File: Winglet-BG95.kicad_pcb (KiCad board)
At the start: 4 copper layers, 30 x 47.6 mm, 43 parts, among them J1 2337019-1, J2 2337019-1, J3 NSIM-16-B, M1 PTH_M2.5, M2 PTH_M2.5, Q1 DMG1012UW-7, Q2 DMG1012UW-7, U1 BG95M1LA, U2 MFF2-SIM, U3 24AA01T-I/OT, U4 FXLA108BQX

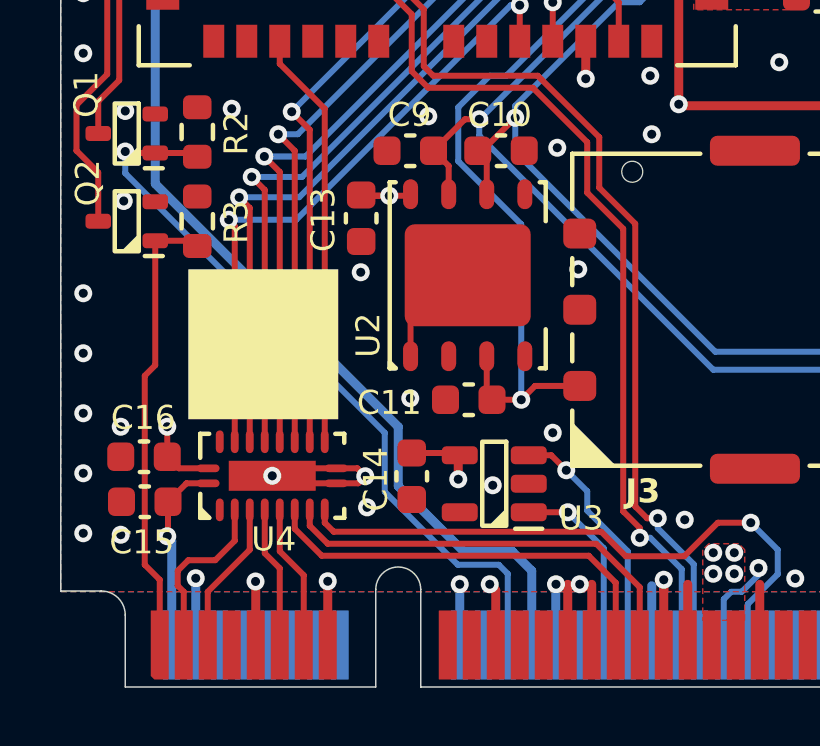
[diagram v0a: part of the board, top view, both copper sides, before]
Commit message: Update export scripts
Change DNF options
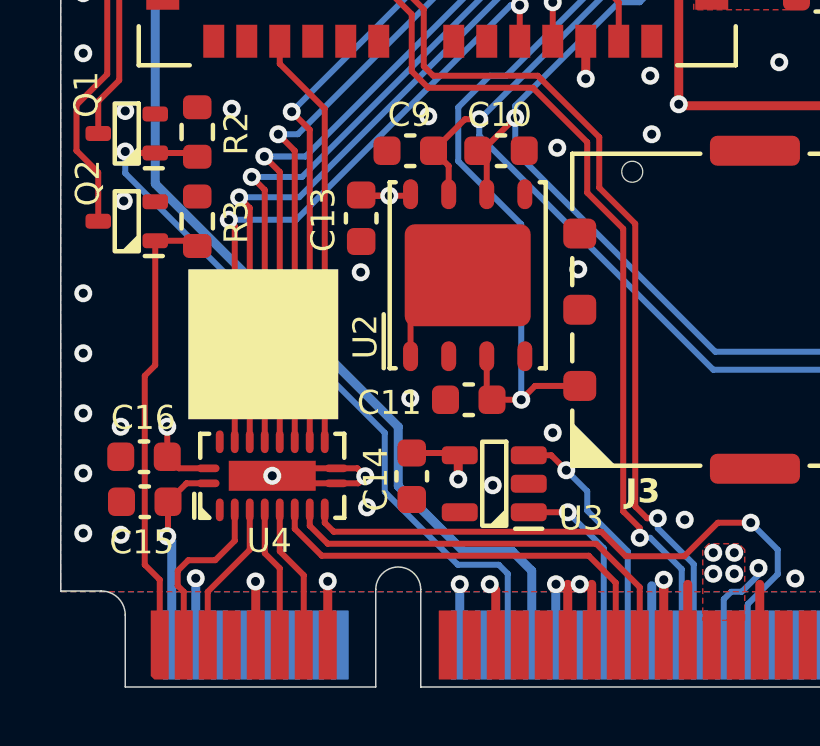
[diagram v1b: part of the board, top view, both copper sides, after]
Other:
- board text added: "Winglet-BG95 v1.1b Jun 25"
- board text removed: "Winglet-BG95 v1.1 Jun 25"
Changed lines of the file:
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@@
 		(title "${LAYER_NAME}")
 		(date "2025-06-05")
-		(rev "v1.1")
+		(rev "v1.1b")
 		(company "TL Embedded")
 	)
@@
 		(at 57.05 93.735 90)
 		(property "Reference" "U4"
-			(at -2.115 0.05 180)
+			(at -2.165 -0.1 180)
 			(layer "F.SilkS")
 			(effects
@@
 		(attr smd)
 		(fp_line
+			(start -0.6 -2.6)
+			(end -1.4 -2.6)
+			(stroke
+				(width 0.15)
+				(type solid)
+			)
+			(layer "F.SilkS")
+		)
+		(fp_line
 			(start 1.4 -2.4)
 			(end 1.4 -2.1)
@@
 		)
 		(fp_line
-			(start 1.1 2.4)
+			(start 0.6 2.4)
 			(end 1.4 2.4)
 			(stroke
@@
 		)
 		(fp_line
-			(start -1.1 2.4)
+			(start -0.7 2.4)
 			(end -1.4 2.4)
 			(stroke
@@
 			)
 		)
-		(property "Description" ""
+		(property "Description" "RF TXRX MOD SMD"
 			(at 0 0 0)
 			(layer "F.Fab")
@@
 		)
 		(embedded_fonts no)
-		(model ":LAMBO_LIB:Step/module/BG95M4LA-64-SGNS.step"
+		(model "${LAMBO_LIB}/Step/module/EG915.STEP"
 			(offset
 				(xyz 0 0 0)
@@
 		(at 63.565 87.05 90)
 		(property "Reference" "U2"
-			(at -2 -3.315 270)
+			(at -2.05 -3.415 270)
 			(layer "F.SilkS")
 			(effects
@@
 		(attr smd dnp)
 		(fp_line
-			(start 3.1 -2.6)
-			(end -3.1 -2.6)
+			(start -1.3 -2.8)
+			(end -3.1 -2.8)
 			(stroke
 				(width 0.15)
@@
 		(fp_line
 			(start 3.1 -2.6)
-			(end 3.1 -2.4)
+			(end -3.1 -2.6)
 			(stroke
 				(width 0.15)
-				(type default)
+				(type solid)
 			)
 			(layer "F.SilkS")
 		)
 		(fp_line
-			(start -3.1 -2.6)
-			(end -3.1 -2.4)
+			(start 3.1 -2.6)
+			(end 3.1 -2.4)
 			(stroke
 				(width 0.15)
@@
 		)
 		(fp_line
-			(start 3.1 2.6)
-			(end 3.1 2.4)
+			(start -3.1 -2.6)
+			(end -3.1 -2.4)
 			(stroke
 				(width 0.15)
@@
 		(fp_line
 			(start 3.1 2.6)
-			(end 1.8 2.6)
+			(end 3.1 2.4)
 			(stroke
 				(width 0.15)
@@
 		(fp_line
 			(start -3.1 2.6)
-			(end -1.8 2.6)
+			(end 3.1 2.6)
 			(stroke
 				(width 0.15)
@@
 			(layer "F.SilkS")
 		)
-		(fp_poly
-			(pts
-				(xy -3.1 -2.6) (xy -3.1 -2.4) (xy -2.9 -2.6)
-			)
-			(stroke
-				(width 0.15)
-				(type solid)
-			)
-			(fill yes)
-			(layer "F.SilkS")
-		)
 		(fp_rect
 			(start -3.4 -2.8)
@@
 		(sheetname "/Translation/")
 		(sheetfile "translation.kicad_sch")
-		(attr smd dnp)
+		(attr smd)
 		(fp_line
 			(start -0.6 -1.16)
@@
 		(sheetname "/Translation/")
 		(sheetfile "translation.kicad_sch")
-		(attr smd dnp)
+		(attr smd)
 		(fp_line
 			(start -0.237258 -0.5225)
@@
 		(layer "Edge.Cuts")
 	)
-	(gr_text "Winglet-BG95\nv1.1\nJun 25"
+	(gr_text "Winglet-BG95\nv1.1b\nJun 25"
 		(at 73.3 56.9 0)
 		(layer "B.SilkS")
